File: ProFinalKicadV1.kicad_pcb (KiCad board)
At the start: 2 copper layers, 25 parts, among them P1 CONN_01X02, P2 CONN_01X02, SW501 SPST, U1 MICRO-B_USB, U2 MIC5219-3.3BM5, U3 FT231XS, U4 XB24-Z7WIT-004

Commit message: PCB
Ruteo de la placa
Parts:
- added G***: LOGO, CESE_pretty:Logo_Poncho, F.Cu at (146.3, 76.5)
- moved C3 41.4 mm to (154.4, 119.9), turned to 90 degrees
- moved C4 29.2 mm to (142.0, 106.7)
- moved P1 26.6 mm to (135.4, 106.7)
- moved U3 26.4 mm to (149.9, 109.5)
- moved D2 24.6 mm to (141.7, 119.6)
- moved SW501 22.0 mm to (153.9, 97.5), turned to 90 degrees
- moved D1 19.6 mm to (141.7, 115.6)
- moved C2 19.4 mm to (156.7, 115.8), turned to 90 degrees
- moved R2 18.9 mm to (147.1, 119.6)
- moved R1 18.7 mm to (147.1, 115.6)
- moved C5 16.9 mm to (147.1, 98.0), turned to 180 degrees
- moved D3 16.5 mm to (136.9, 93.2), turned to 0 degrees
- moved C1 16.2 mm to (137.9, 111.0)
- moved C6 14.1 mm to (140.2, 102.1), turned to 180 degrees
- moved U2 13.7 mm to (135.4, 101.9)
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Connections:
- C4 pad 1: (no net) -> Net-(C4-Pad1)
- D1 pad 1: (no net) -> Net-(D1-Pad1)
- D2 pad 1: (no net) -> Net-(D2-Pad1)
- R3 pad 2: (no net) -> Net-(R3-Pad2)
- R4 pad 2: (no net) -> Net-(R4-Pad2)
- U4 pad 12: (no net) -> Net-(U3-PadP6)
- U4 pad 16: (no net) -> Net-(U3-PadP19)
- U4 pad 9: (no net) -> /DTS_DTR_XBEE
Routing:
- net GND: track 0.00 -> 134.1 mm, vias 0 -> 1
- net +3V3: track 0.00 -> 109.2 mm
- net +5V: track 0.00 -> 107.0 mm, vias 0 -> 1
- net /DIN: track 0.00 -> 60.9 mm, vias 0 -> 1
- net /DOUT: track 0.00 -> 56.2 mm, vias 0 -> 1
- net Net-(U3-PadP19): track 0.00 -> 54.4 mm
- net Net-(C4-Pad1): track 0.00 -> 43.6 mm, vias 0 -> 2
- net Net-(U3-PadP6): track 0.00 -> 42.7 mm, vias 0 -> 1
- net /D+: track 0.00 -> 27.6 mm
- net /DTS_DTR_XBEE: track 0.00 -> 27.6 mm, vias 0 -> 1
- net /D-: track 0.00 -> 26.6 mm, vias 0 -> 2
- net Net-(SW501-Pad2): track 0.00 -> 25.6 mm
- net Net-(D2-Pad1): track 0.00 -> 22.3 mm
- net Net-(D1-Pad1): track 0.00 -> 16.6 mm
- net Net-(XA1-Pad20): track 0.00 -> 15.2 mm
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
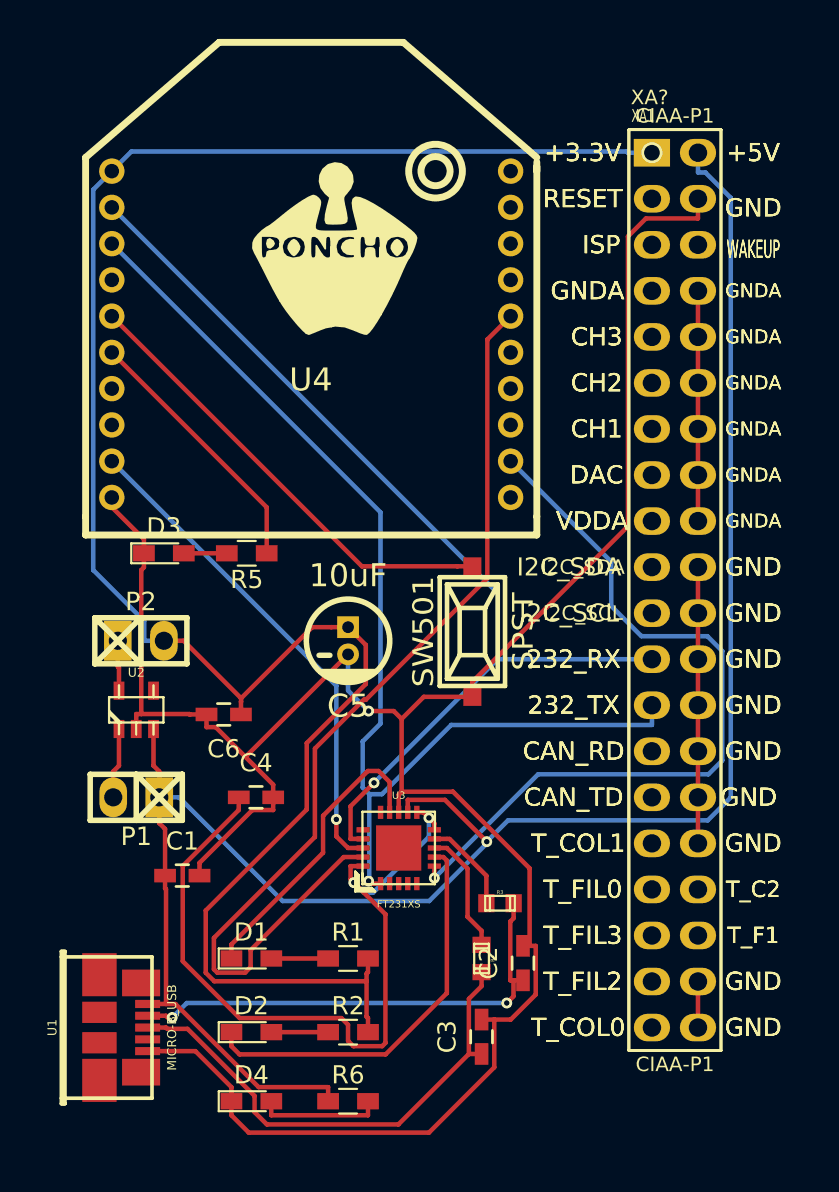
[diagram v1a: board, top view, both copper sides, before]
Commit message: Relleno Zona GND
Relleno GND
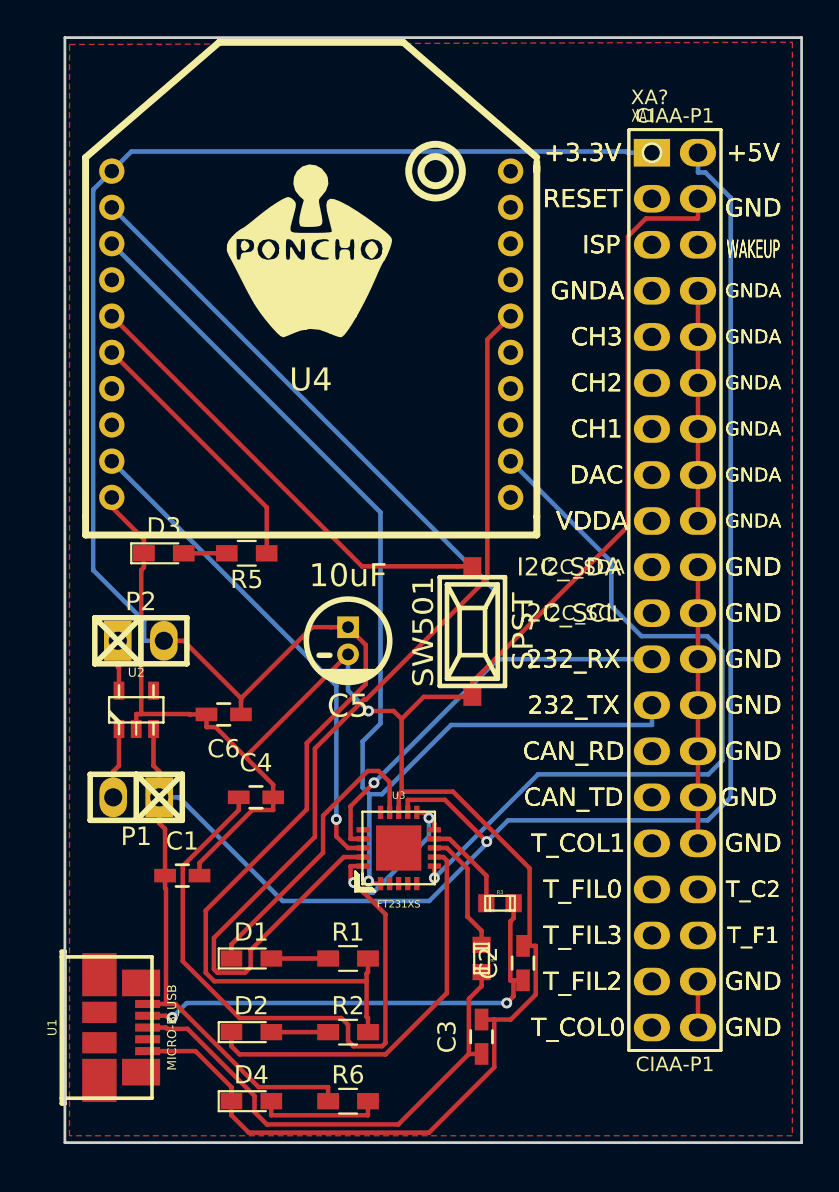
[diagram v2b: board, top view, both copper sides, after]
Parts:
- moved G*** 1.40 mm to (144.9, 76.6)
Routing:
- added copper zone on F.Cu, net GND
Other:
- board outline added: 40.6 x 61 mm
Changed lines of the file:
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@@
     (links 63)
     (no_connects 0)
-    (area 130.149244 64.494999 172.360001 126.069)
+    (area 131.369999 64.694999 172.160001 125.805001)
     (thickness 1.6)
-    (drawings 0)
+    (drawings 4)
     (tracks 275)
     (zones 0)
@@
     (0 F.Cu signal)
     (31 B.Cu signal)
-    (32 B.Adhes user)
+    (32 B.Adhes user hide)
     (33 F.Adhes user)
-    (34 B.Paste user)
-    (35 F.Paste user)
-    (36 B.SilkS user)
+    (34 B.Paste user hide)
+    (35 F.Paste user hide)
+    (36 B.SilkS user hide)
     (37 F.SilkS user)
-    (38 B.Mask user)
-    (39 F.Mask user)
+    (38 B.Mask user hide)
+    (39 F.Mask user hide)
     (40 Dwgs.User user)
-    (41 Cmts.User user)
-    (42 Eco1.User user)
-    (43 Eco2.User user)
+    (41 Cmts.User user hide)
+    (42 Eco1.User user hide)
+    (43 Eco2.User user hide)
     (44 Edge.Cuts user)
-    (45 Margin user)
-    (46 B.CrtYd user)
-    (47 F.CrtYd user)
-    (48 B.Fab user)
-    (49 F.Fab user)
+    (45 Margin user hide)
+    (46 B.CrtYd user hide)
+    (47 F.CrtYd user hide)
+    (48 B.Fab user hide)
+    (49 F.Fab user hide)
   )
   (setup
@@
   )
   (module CESE_pretty:Logo_Poncho (layer F.Cu)
-    (at 146.304 76.454)
+    (at 144.907 76.581)
     (fp_text reference G*** (at 0.127 5.588) (layer F.SilkS) hide
       (effects (font (thickness 0.3)))
@@
       (xy 3.778435 -0.1467) (xy 3.778435 -0.1467)) (layer F.SilkS) (width 0.1))
   )
+  (gr_line (start 131.445 125.73) (end 172.085 125.73) (angle 90) (layer Edge.Cuts) (width 0.15))
+  (gr_line (start 131.445 64.77) (end 131.445 125.73) (angle 90) (layer Edge.Cuts) (width 0.15))
+  (gr_line (start 172.085 64.77) (end 131.445 64.77) (angle 90) (layer Edge.Cuts) (width 0.15))
+  (gr_line (start 172.085 125.73) (end 172.085 64.77) (angle 90) (layer Edge.Cuts) (width 0.15))
   (via (at 154.7173 109.1255) (size 0.6) (layers F.Cu B.Cu) (net 1))
   (segment (start 136.652 106.68) (end 136.652 108.1051) (width 0.25) (layer F.Cu) (net 1))
@@
   (segment (start 147.0649 109.474) (end 146.4202 108.8293) (width 0.25) (layer F.Cu) (net 26))
   (segment (start 147.894 109.474) (end 147.0649 109.474) (width 0.25) (layer F.Cu) (net 26))
+  (zone (net 2) (net_name GND) (layer F.Cu) (hatch edge 0.508)
+    (connect_pads (clearance 0.508))
+    (min_thickness 0.254)
+    (fill yes (arc_segments 16) (thermal_gap 0.508) (thermal_bridge_width 0.508))
+    (polygon
+      (pts
+        (xy 171.577 125.349) (xy 131.699 125.349) (xy 131.699 65.151) (xy 171.577 65.024)
+      )
+    )
+  )
 )
